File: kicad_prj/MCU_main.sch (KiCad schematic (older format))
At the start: 1 part

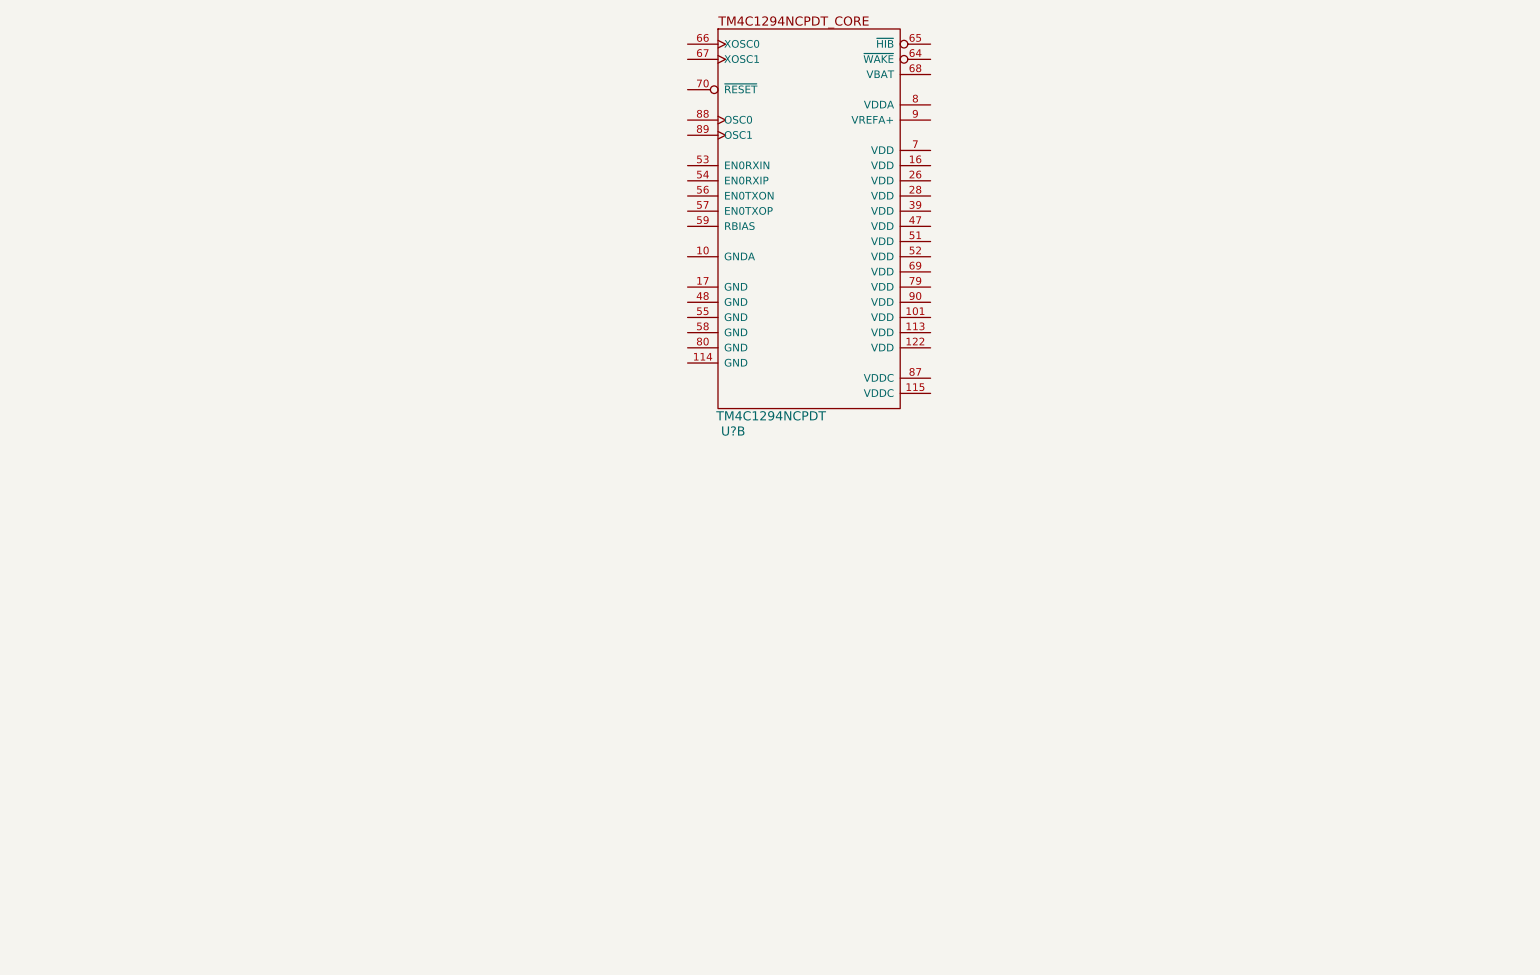
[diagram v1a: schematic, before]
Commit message: Ethernet and decoupling capacitors
Change ethernet jack symbol to add LEDs.
Change all sheets to have power inputs tied to a global label instead of
sheet pins.
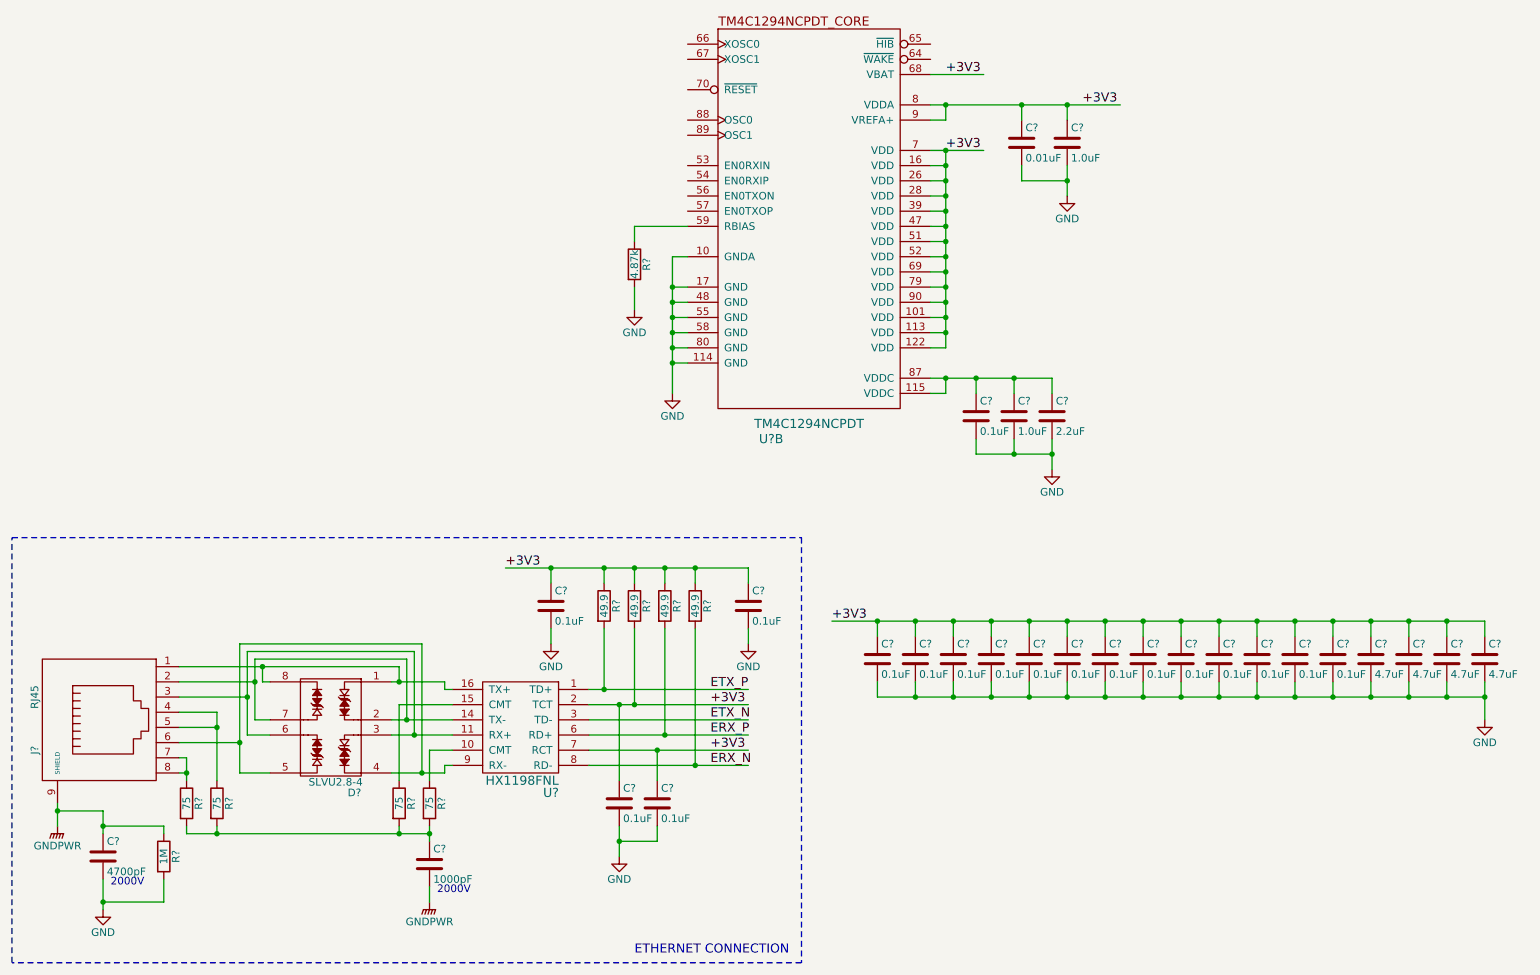
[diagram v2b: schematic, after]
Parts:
- removed U?: TM4C1294NCPDT, symbol TM4C1294NCPDT
- added C? (x18): 0.1uF, symbol C
- added C? (x2): 1.0uF, symbol C
- added C?: 2.2uF, symbol C
- added C? (x4): 4.7uF, symbol C
- added C?: 0.01uF, symbol C
- added C?: 1000pF, symbol C
- added C?: 4700pF, symbol C
- added D?: SLVU2.8-4, symbol SLVU2.8-4
- added J?: RJ45, symbol RJ45
- added R?: 4.87k, symbol R
- added R? (x4): 49.9, symbol R
- added R? (x4): 75, symbol R
- added R?: 1M, symbol R
- added U?: HX1198FNL, symbol HX1198FNL
- added U?: TM4C1294NCPDT, symbol TM4C1294NCPDT
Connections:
- net labels added: +3V3, ERX_N, ERX_P, ETX_N, ETX_P, GND, GNDPWR
- wire segments 0 -> 156
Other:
- note added: "2000V"
- note added: "ETHERNET CONNECTION"
